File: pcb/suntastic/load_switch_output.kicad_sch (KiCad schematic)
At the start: 1 part, among them U6 TPS22917DBV

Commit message: Rename sheet
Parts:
- added J1: Screw_Terminal_01x02, symbol Connector:Screw_Terminal_01x02
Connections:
- net GND: now reaches U6.2 (GND)
- net GND: now also J1.2 (Pin_2)
- net at U6.6 (VOUT): now also J1.1 (Pin_1)
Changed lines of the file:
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@@
     (rev "1")
+  )
+  (junction (at 78.74 49.53) (diameter 0) (color 0 0 0 0)
+  )
+  (wire (pts (xy 78.74 49.53) (xy 91.44 49.53))
+    (stroke (width 0) (type default))
+  )
+  (wire (pts (xy 67.31 49.53) (xy 78.74 49.53))
+    (stroke (width 0) (type default))
+  )
+  (wire (pts (xy 77.47 39.37) (xy 91.44 39.37))
+    (stroke (width 0) (type default))
+  )
+  (wire (pts (xy 91.44 49.53) (xy 91.44 41.91))
+    (stroke (width 0) (type default))
   )
   (wire (pts (xy 54.61 44.45) (xy 57.15 44.45))
@@
         )
       )
+    )
+  )
+  (symbol (lib_id "power:GND") (at 78.74 49.53 0) (unit 1)
+    (in_bom yes) (on_board yes) (dnp no) (fields_autoplaced)
+    (property "Reference" "#PWR023" (at 78.74 55.88 0)
+      (effects (font (size 1.27 1.27)) hide)
+    )
+    (property "Value" "GND" (at 78.74 54.61 0)
+      (effects (font (size 1.27 1.27)))
+    )
+    (property "Footprint" "" (at 78.74 49.53 0)
+      (effects (font (size 1.27 1.27)) hide)
+    )
+    (property "Datasheet" "" (at 78.74 49.53 0)
+      (effects (font (size 1.27 1.27)) hide)
+    )
+    (pin "1")
+    (instances
+      (project "suntastic"
+        (path "/4d5a6178-89d6-4824-ac30-5dee40aabff2/18707a27-b221-4259-b1c0-1b578b6ae71d"
+          (reference "#PWR023") (unit 1)
+        )
+      )
+    )
+  )
+  (symbol (lib_id "Connector:Screw_Terminal_01x02") (at 96.52 39.37 0) (unit 1)
+    (in_bom yes) (on_board yes) (dnp no) (fields_autoplaced)
+    (property "Reference" "J1" (at 99.06 40.005 0)
+      (effects (font (size 1.27 1.27)) (justify left))
+    )
+    (property "Value" "Screw_Terminal_01x02" (at 99.06 42.545 0)
+      (effects (font (size 1.27 1.27)) (justify left))
+    )
+    (property "Footprint" "" (at 96.52 39.37 0)
+      (effects (font (size 1.27 1.27)) hide)
+    )
+    (property "Datasheet" "~" (at 96.52 39.37 0)
+      (effects (font (size 1.27 1.27)) hide)
+    )
+    (pin "1")
+    (pin "2")
+    (instances
+      (project "suntastic"
+        (path "/4d5a6178-89d6-4824-ac30-5dee40aabff2/18707a27-b221-4259-b1c0-1b578b6ae71d"
+          (reference "J1") (unit 1)
+        )
+      )

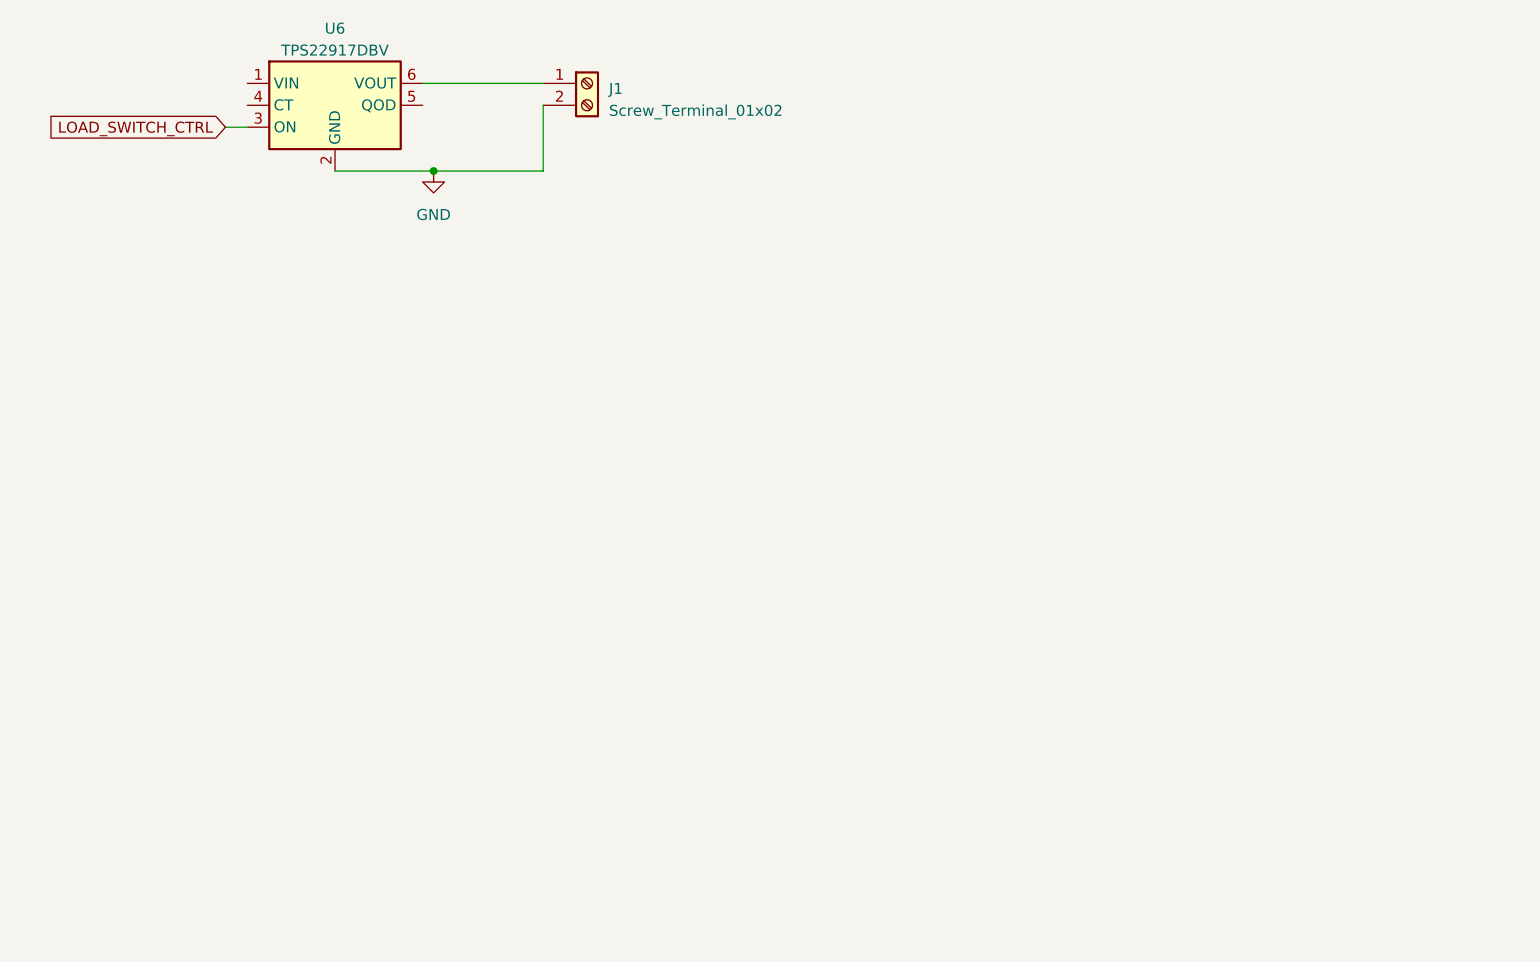
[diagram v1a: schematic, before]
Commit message: Add load switch and RAK connector
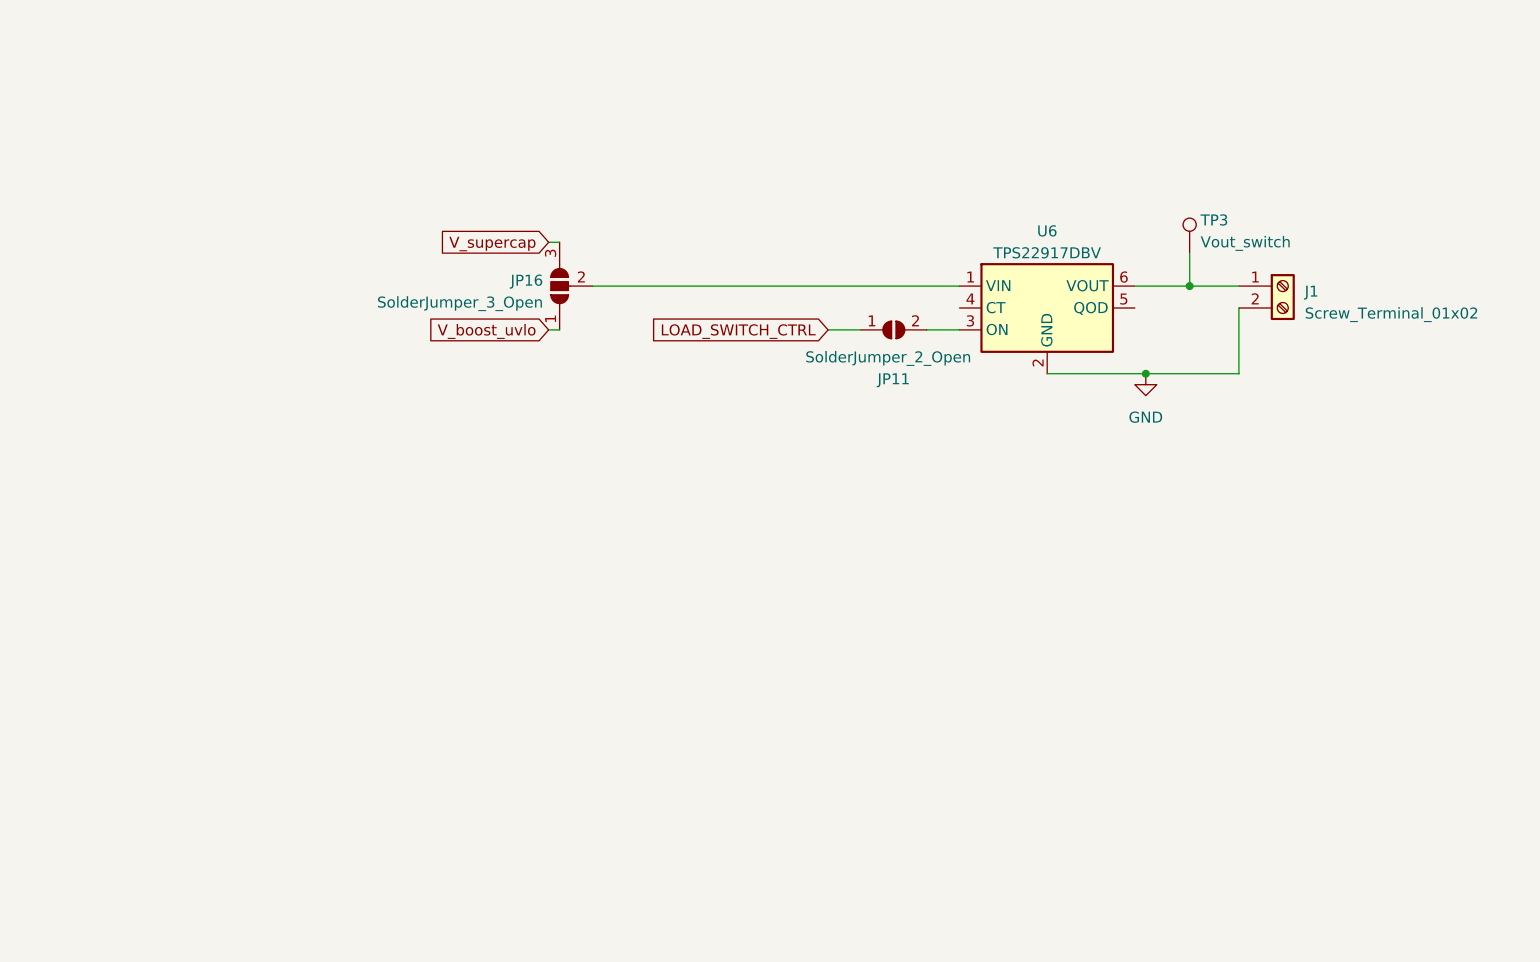
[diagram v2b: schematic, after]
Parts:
- added JP11: SolderJumper_2_Open, Jumper:SolderJumper-2_P1.3mm_Open_RoundedPad1.0x1.5mm, symbol Jumper:SolderJumper_2_Open
- added JP16: SolderJumper_3_Open, Jumper:SolderJumper-3_P1.3mm_Open_RoundedPad1.0x1.5mm, symbol Jumper:SolderJumper_3_Open
- added TP3: Vout_switch, symbol Connector:TestPoint
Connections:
- net LOAD_SWITCH_CTRL: now also JP11.1 (A); no longer U6.3 (ON)
- net at U6.1 (VIN): now also JP16.2 (C)
- net at J1.1 (Pin_1), U6.6 (VOUT): now also TP3.1
- new net: JP11.2 (B), U6.3 (ON)
- new net V_boost_uvlo: JP16.1 (A)
- new net V_supercap: JP16.3 (B)
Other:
- moved on the sheet: J1, U6
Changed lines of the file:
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@@
     (date "2024-02-07")
     (rev "1")
-  )
-  (junction (at 78.74 49.53) (diameter 0) (color 0 0 0 0)
-  )
-  (wire (pts (xy 78.74 49.53) (xy 91.44 49.53))
-    (stroke (width 0) (type default))
-  )
-  (wire (pts (xy 67.31 49.53) (xy 78.74 49.53))
-    (stroke (width 0) (type default))
-  )
-  (wire (pts (xy 77.47 39.37) (xy 91.44 39.37))
-    (stroke (width 0) (type default))
-  )
-  (wire (pts (xy 91.44 49.53) (xy 91.44 41.91))
-    (stroke (width 0) (type default))
-  )
-  (wire (pts (xy 54.61 44.45) (xy 57.15 44.45))
-    (stroke (width 0) (type default))
-  )
-  (global_label "LOAD_SWITCH_CTRL" (shape input) (at 54.61 44.45 180) (fields_autoplaced)
+    (comment 1 "This block is in charge of powering ON or OFF the load based on the status of the UVLO")
+  )
+  (junction (at 166.37 62.865) (diameter 0) (color 0 0 0 0)
+  )
+  (junction (at 161.29 73.025) (diameter 0) (color 0 0 0 0)
+  )
+  (wire (pts (xy 166.37 59.055) (xy 166.37 62.865))
+    (stroke (width 0) (type default))
+  )
+  (wire (pts (xy 161.29 73.025) (xy 172.085 73.025))
+    (stroke (width 0) (type default))
+  )
+  (wire (pts (xy 97.155 62.865) (xy 139.7 62.865))
+    (stroke (width 0) (type default))
+  )
+  (wire (pts (xy 149.86 73.025) (xy 161.29 73.025))
+    (stroke (width 0) (type default))
+  )
+  (wire (pts (xy 92.075 67.945) (xy 93.345 67.945))
+    (stroke (width 0) (type default))
+  )
+  (wire (pts (xy 160.02 62.865) (xy 166.37 62.865))
+    (stroke (width 0) (type default))
+  )
+  (wire (pts (xy 92.075 57.785) (xy 93.345 57.785))
+    (stroke (width 0) (type default))
+  )
+  (wire (pts (xy 135.89 67.945) (xy 139.7 67.945))
+    (stroke (width 0) (type default))
+  )
+  (wire (pts (xy 172.085 73.025) (xy 172.085 65.405))
+    (stroke (width 0) (type default))
+  )
+  (wire (pts (xy 124.46 67.945) (xy 128.27 67.945))
+    (stroke (width 0) (type default))
+  )
+  (wire (pts (xy 166.37 62.865) (xy 172.085 62.865))
+    (stroke (width 0) (type default))
+  )
+  (global_label "V_supercap" (shape input) (at 92.075 57.785 180) (fields_autoplaced)
     (effects (font (size 1.27 1.27)) (justify right))
-    (property "Intersheetrefs" "${INTERSHEET_REFS}" (at 33.6823 44.45 0)
+    (property "Intersheetrefs" "${INTERSHEET_REFS}" (at 78.5255 57.785 0)
       (effects (font (size 1.27 1.27)) (justify right) hide)
     )
   )
-  (symbol (lib_id "Power_Management:TPS22917DBV") (at 67.31 41.91 0) (unit 1)
-    (in_bom yes) (on_board yes) (dnp no) (fields_autoplaced)
-    (property "Reference" "U6" (at 67.31 33.02 0)
-      (effects (font (size 1.27 1.27)))
-    )
-    (property "Value" "TPS22917DBV" (at 67.31 35.56 0)
-      (effects (font (size 1.27 1.27)))
-    )
-    (property "Footprint" "Package_TO_SOT_SMD:SOT-23-6" (at 67.31 29.21 0)
-      (effects (font (size 1.27 1.27)) hide)
-    )
-    (property "Datasheet" "http://www.ti.com/lit/ds/symlink/tps22917.pdf" (at 68.58 59.69 0)
+  (global_label "V_boost_uvlo" (shape input) (at 92.075 67.945 180) (fields_autoplaced)
+    (effects (font (size 1.27 1.27)) (justify right))
+    (property "Intersheetrefs" "${INTERSHEET_REFS}" (at 77.0138 67.945 0)
+      (effects (font (size 1.27 1.27)) (justify right) hide)
+    )
+  )
+  (global_label "LOAD_SWITCH_CTRL" (shape input) (at 124.46 67.945 180) (fields_autoplaced)
+    (effects (font (size 1.27 1.27)) (justify right))
+    (property "Intersheetrefs" "${INTERSHEET_REFS}" (at 103.5323 67.945 0)
+      (effects (font (size 1.27 1.27)) (justify right) hide)
+    )
+  )
+  (symbol (lib_id "Power_Management:TPS22917DBV") (at 149.86 65.405 0) (unit 1)
+    (in_bom yes) (on_board yes) (dnp no) (fields_autoplaced)
+    (property "Reference" "U6" (at 149.86 56.515 0)
+      (effects (font (size 1.27 1.27)))
+    )
+    (property "Value" "TPS22917DBV" (at 149.86 59.055 0)
+      (effects (font (size 1.27 1.27)))
+    )
+    (property "Footprint" "Package_TO_SOT_SMD:SOT-23-6" (at 149.86 52.705 0)
+      (effects (font (size 1.27 1.27)) hide)
+    )
+    (property "Datasheet" "http://www.ti.com/lit/ds/symlink/tps22917.pdf" (at 151.13 83.185 0)
       (effects (font (size 1.27 1.27)) hide)
     )
@@
     )
   )
-  (symbol (lib_id "power:GND") (at 78.74 49.53 0) (unit 1)
-    (in_bom yes) (on_board yes) (dnp no) (fields_autoplaced)
-    (property "Reference" "#PWR023" (at 78.74 55.88 0)
-      (effects (font (size 1.27 1.27)) hide)
-    )
-    (property "Value" "GND" (at 78.74 54.61 0)
-      (effects (font (size 1.27 1.27)))
-    )
-    (property "Footprint" "" (at 78.74 49.53 0)
-      (effects (font (size 1.27 1.27)) hide)
-    )
-    (property "Datasheet" "" (at 78.74 49.53 0)
+  (symbol (lib_id "Connector:TestPoint") (at 166.37 59.055 0) (unit 1)
+    (in_bom yes) (on_board yes) (dnp no)
+    (property "Reference" "TP3" (at 167.64 55.245 0)
+      (effects (font (size 1.27 1.27)) (justify left))
+    )
+    (property "Value" "Vout_switch" (at 167.64 57.785 0)
+      (effects (font (size 1.27 1.27)) (justify left))
+    )
+    (property "Footprint" "" (at 171.45 59.055 0)
+      (effects (font (size 1.27 1.27)) hide)
+    )
+    (property "Datasheet" "~" (at 171.45 59.055 0)
+      (effects (font (size 1.27 1.27)) hide)
+    )
+    (pin "1")
+    (instances
+      (project "suntastic"
+        (path "/4d5a6178-89d6-4824-ac30-5dee40aabff2/18707a27-b221-4259-b1c0-1b578b6ae71d"
+          (reference "TP3") (unit 1)
+        )
+      )
+    )
+  )
+  (symbol (lib_id "power:GND") (at 161.29 73.025 0) (unit 1)
+    (in_bom yes) (on_board yes) (dnp no) (fields_autoplaced)
+    (property "Reference" "#PWR023" (at 161.29 79.375 0)
+      (effects (font (size 1.27 1.27)) hide)
+    )
+    (property "Value" "GND" (at 161.29 78.105 0)
+      (effects (font (size 1.27 1.27)))
+    )
+    (property "Footprint" "" (at 161.29 73.025 0)
+      (effects (font (size 1.27 1.27)) hide)
+    )
+    (property "Datasheet" "" (at 161.29 73.025 0)
       (effects (font (size 1.27 1.27)) hide)
     )
@@
     )
   )
-  (symbol (lib_id "Connector:Screw_Terminal_01x02") (at 96.52 39.37 0) (unit 1)
-    (in_bom yes) (on_board yes) (dnp no) (fields_autoplaced)
-    (property "Reference" "J1" (at 99.06 40.005 0)
-      (effects (font (size 1.27 1.27)) (justify left))
-    )
-    (property "Value" "Screw_Terminal_01x02" (at 99.06 42.545 0)
-      (effects (font (size 1.27 1.27)) (justify left))
-    )
-    (property "Footprint" "" (at 96.52 39.37 0)
-      (effects (font (size 1.27 1.27)) hide)
-    )
-    (property "Datasheet" "~" (at 96.52 39.37 0)
+  (symbol (lib_id "Connector:Screw_Terminal_01x02") (at 177.165 62.865 0) (unit 1)
+    (in_bom yes) (on_board yes) (dnp no) (fields_autoplaced)
+    (property "Reference" "J1" (at 179.705 63.5 0)
+      (effects (font (size 1.27 1.27)) (justify left))
+    )
+    (property "Value" "Screw_Terminal_01x02" (at 179.705 66.04 0)
+      (effects (font (size 1.27 1.27)) (justify left))
+    )
+    (property "Footprint" "" (at 177.165 62.865 0)
+      (effects (font (size 1.27 1.27)) hide)
+    )
+    (property "Datasheet" "~" (at 177.165 62.865 0)
       (effects (font (size 1.27 1.27)) hide)
     )
@@
         )
       )
+    )
+  )
+  (symbol (lib_id "Jumper:SolderJumper_2_Open") (at 132.08 67.945 0) (unit 1)
+    (in_bom yes) (on_board yes) (dnp no)
+    (property "Reference" "JP11" (at 132.08 73.66 0)
+      (effects (font (size 1.27 1.27)))
+    )
+    (property "Value" "SolderJumper_2_Open" (at 131.445 71.12 0)
+      (effects (font (size 1.27 1.27)))
+    )
+    (property "Footprint" "Jumper:SolderJumper-2_P1.3mm_Open_RoundedPad1.0x1.5mm" (at 132.08 67.945 0)
+      (effects (font (size 1.27 1.27)) hide)
+    )
+    (property "Datasheet" "~" (at 132.08 67.945 0)
+      (effects (font (size 1.27 1.27)) hide)
+    )
+    (pin "1")
+    (pin "2")
+    (instances
+      (project "suntastic"
+        (path "/4d5a6178-89d6-4824-ac30-5dee40aabff2/49b74624-bdf8-42ea-a5aa-f04e40ea326b"
+          (reference "JP11") (unit 1)
+        )
+        (path "/4d5a6178-89d6-4824-ac30-5dee40aabff2/18707a27-b221-4259-b1c0-1b578b6ae71d"
+          (reference "JP15") (unit 1)
+        )
+      )
+    )
+  )
+  (symbol (lib_id "Jumper:SolderJumper_3_Open") (at 93.345 62.865 90) (unit 1)
+    (in_bom yes) (on_board yes) (dnp no) (fields_autoplaced)
+    (property "Reference" "JP16" (at 91.44 62.23 90)
+      (effects (font (size 1.27 1.27)) (justify left))
+    )
+    (property "Value" "SolderJumper_3_Open" (at 91.44 64.77 90)
+      (effects (font (size 1.27 1.27)) (justify left))
+    )
+    (property "Footprint" "Jumper:SolderJumper-3_P1.3mm_Open_RoundedPad1.0x1.5mm" (at 93.345 62.865 0)
+      (effects (font (size 1.27 1.27)) hide)
+    )
+    (property "Datasheet" "~" (at 93.345 62.865 0)
+      (effects (font (size 1.27 1.27)) hide)
+    )
+    (pin "1")
+    (pin "2")
+    (pin "3")
+    (instances
+      (project "suntastic"
+        (path "/4d5a6178-89d6-4824-ac30-5dee40aabff2/18707a27-b221-4259-b1c0-1b578b6ae71d"
+          (reference "JP16") (unit 1)
+        )
+      )

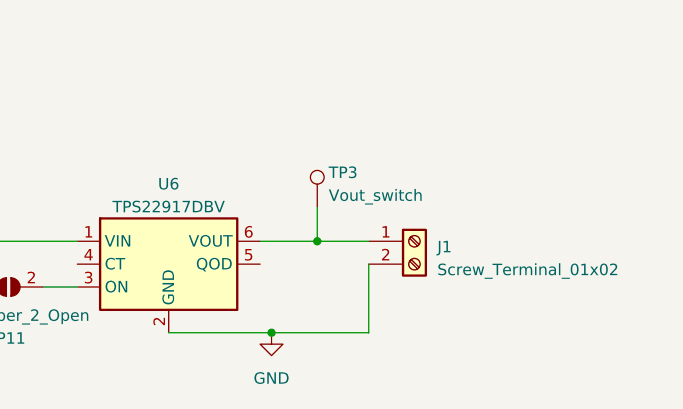
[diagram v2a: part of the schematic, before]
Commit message: Add more doccstrings
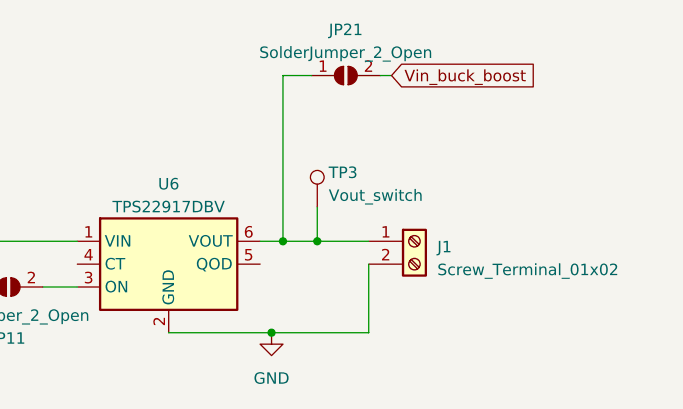
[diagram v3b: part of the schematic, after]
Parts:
- added JP21: SolderJumper_2_Open, symbol Jumper:SolderJumper_2_Open
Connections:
- net at J1.1 (Pin_1), TP3.1, U6.6 (VOUT): now also JP21.1 (A)
- new net Vin_buck_boost: JP21.2 (B)
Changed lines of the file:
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@@
   (junction (at 161.29 73.025) (diameter 0) (color 0 0 0 0)
+  )
+  (junction (at 162.56 62.865) (diameter 0) (color 0 0 0 0)
   )
   (wire (pts (xy 166.37 59.055) (xy 166.37 62.865))
@@
     (stroke (width 0) (type default))
   )
-  (wire (pts (xy 160.02 62.865) (xy 166.37 62.865))
+  (wire (pts (xy 160.02 62.865) (xy 162.56 62.865))
     (stroke (width 0) (type default))
   )
@@
     (stroke (width 0) (type default))
   )
+  (wire (pts (xy 162.56 62.865) (xy 166.37 62.865))
+    (stroke (width 0) (type default))
+  )
+  (wire (pts (xy 165.735 44.45) (xy 162.56 44.45))
+    (stroke (width 0) (type default))
+  )
+  (wire (pts (xy 162.56 44.45) (xy 162.56 62.865))
+    (stroke (width 0) (type default))
+  )
   (wire (pts (xy 124.46 67.945) (xy 128.27 67.945))
+    (stroke (width 0) (type default))
+  )
+  (wire (pts (xy 173.355 44.45) (xy 174.625 44.45))
     (stroke (width 0) (type default))
   )
@@
     (property "Intersheetrefs" "${INTERSHEET_REFS}" (at 77.0138 67.945 0)
       (effects (font (size 1.27 1.27)) (justify right) hide)
+    )
+  )
+  (global_label "Vin_buck_boost" (shape input) (at 174.625 44.45 0) (fields_autoplaced)
+    (effects (font (size 1.27 1.27)) (justify left))
+    (property "Intersheetrefs" "${INTERSHEET_REFS}" (at 191.9239 44.45 0)
+      (effects (font (size 1.27 1.27)) (justify left) hide)
     )
   )
@@
         )
       )
+    )
+  )
+  (symbol (lib_id "Jumper:SolderJumper_2_Open") (at 169.545 44.45 0) (unit 1)
+    (in_bom yes) (on_board yes) (dnp no) (fields_autoplaced)
+    (property "Reference" "JP21" (at 169.545 39.37 0)
+      (effects (font (size 1.27 1.27)))
+    )
+    (property "Value" "SolderJumper_2_Open" (at 169.545 41.91 0)
+      (effects (font (size 1.27 1.27)))
+    )
+    (property "Footprint" "" (at 169.545 44.45 0)
+      (effects (font (size 1.27 1.27)) hide)
+    )
+    (property "Datasheet" "~" (at 169.545 44.45 0)
+      (effects (font (size 1.27 1.27)) hide)
+    )
+    (pin "1")
+    (pin "2")
+    (instances
+      (project "suntastic"
+        (path "/4d5a6178-89d6-4824-ac30-5dee40aabff2/18707a27-b221-4259-b1c0-1b578b6ae71d"
+          (reference "JP21") (unit 1)
+        )
+      )
